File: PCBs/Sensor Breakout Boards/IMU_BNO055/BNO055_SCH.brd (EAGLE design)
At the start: 25.4 x 25.4 mm, 6 parts

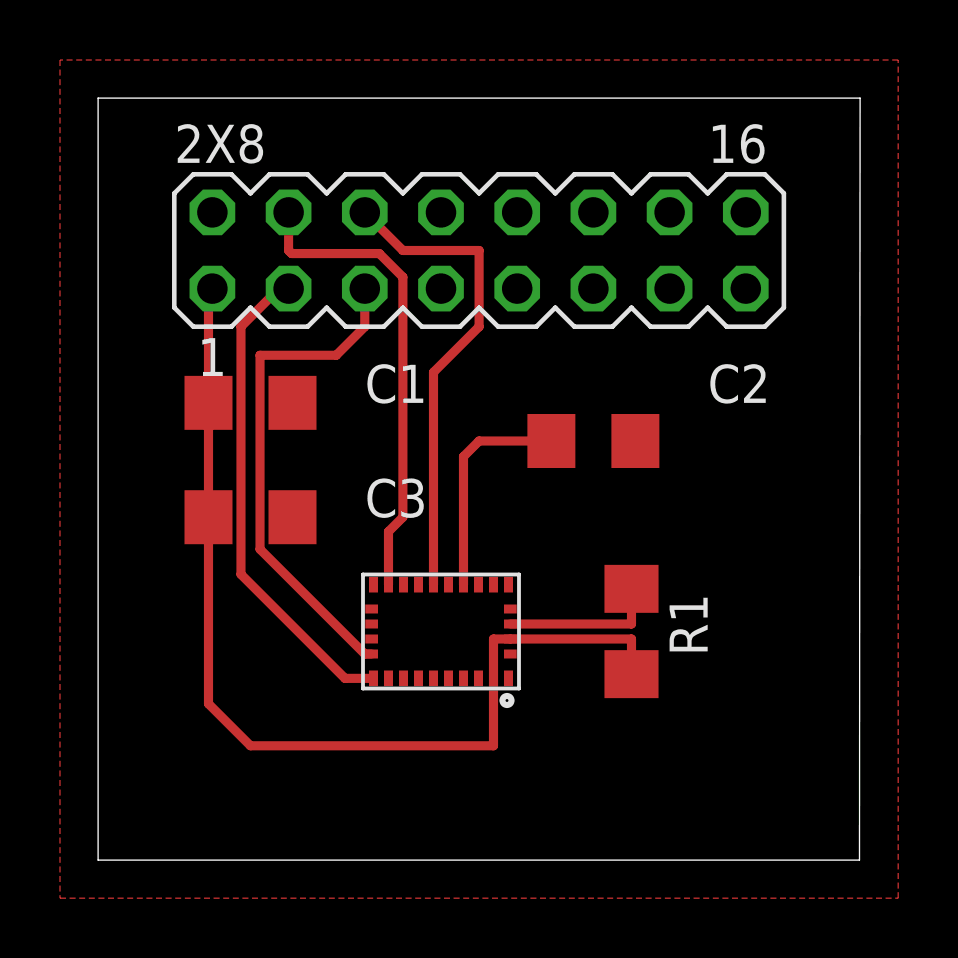
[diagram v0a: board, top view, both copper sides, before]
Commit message: Moved the caps to actually be useful
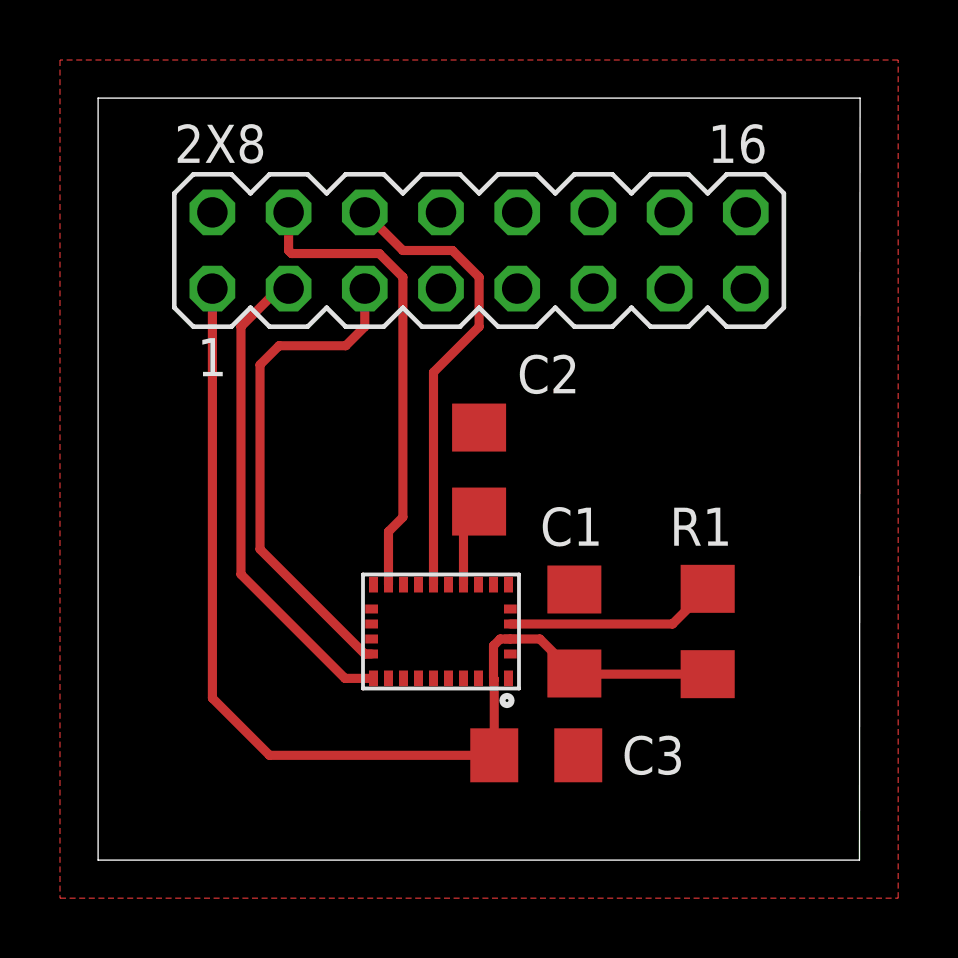
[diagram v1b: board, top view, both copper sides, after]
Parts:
- moved C1 13.2 mm to (15.9, 7.62), turned to 90 degrees
- moved C3 12.4 mm to (14.6, 3.49)
- moved C2 3.93 mm to (12.7, 13.0), turned to 90 degrees
- moved R1 2.54 mm to (20.3, 7.62)
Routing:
- net N$3: track 7.41 -> 2.65 mm
- net BOOT: track 5.21 -> 7.06 mm
- net VCC: track 33.4 -> 35.2 mm
- net RST: track 16.1 -> 15.6 mm
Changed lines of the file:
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@@
 <attribute name="VALUE" x="12.7" y="16.129" size="1.27" layer="27" ratio="10"/>
 </element>
-<element name="C1" library="rcl" library_urn="urn:adsk.eagle:library:334" package="C1206" package3d_urn="urn:adsk.eagle:package:23618/2" value="0.1 uF" x="5.08" y="15.24" smashed="yes">
-<attribute name="NAME" x="8.89" y="15.24" size="1.27" layer="25"/>
-<attribute name="POPULARITY" value="24" x="22.86" y="-6.35" size="1.778" layer="27" display="off"/>
-<attribute name="SPICEPREFIX" value="C" x="22.86" y="-6.35" size="1.778" layer="27" display="off"/>
-<attribute name="VALUE" x="-2.54" y="15.24" size="1.27" layer="27"/>
+<element name="C1" library="rcl" library_urn="urn:adsk.eagle:library:334" package="C1206" package3d_urn="urn:adsk.eagle:package:23618/2" value="0.1 uF" x="15.875" y="7.62" smashed="yes" rot="R90">
+<attribute name="NAME" x="16.8275" y="11.7475" size="1.27" layer="25" rot="R180"/>
+<attribute name="POPULARITY" value="24" x="37.465" y="25.4" size="1.778" layer="27" rot="R90" display="off"/>
+<attribute name="SPICEPREFIX" value="C" x="37.465" y="25.4" size="1.778" layer="27" rot="R90" display="off"/>
+<attribute name="VALUE" x="15.875" y="0" size="1.27" layer="27" rot="R90"/>
 </element>
-<element name="C2" library="rcl" library_urn="urn:adsk.eagle:library:334" package="C1206" package3d_urn="urn:adsk.eagle:package:23618/2" value="1 uF" x="16.51" y="13.97" smashed="yes">
-<attribute name="NAME" x="20.32" y="15.24" size="1.27" layer="25"/>
-<attribute name="POPULARITY" value="24" x="40.64" y="-7.62" size="1.778" layer="27" display="off"/>
-<attribute name="SPICEPREFIX" value="C" x="40.64" y="-7.62" size="1.778" layer="27" display="off"/>
-<attribute name="VALUE" x="20.32" y="13.97" size="1.27" layer="27"/>
+<element name="C2" library="rcl" library_urn="urn:adsk.eagle:library:334" package="C1206" package3d_urn="urn:adsk.eagle:package:23618/2" value="1 uF" x="12.7" y="13.0175" smashed="yes" rot="R90">
+<attribute name="NAME" x="13.97" y="15.5575" size="1.27" layer="25"/>
+<attribute name="POPULARITY" value="24" x="34.29" y="37.1475" size="1.778" layer="27" rot="R90" display="off"/>
+<attribute name="SPICEPREFIX" value="C" x="34.29" y="37.1475" size="1.778" layer="27" rot="R90" display="off"/>
+<attribute name="VALUE" x="12.7" y="16.8275" size="1.27" layer="27" rot="R90"/>
 </element>
-<element name="C3" library="rcl" library_urn="urn:adsk.eagle:library:334" package="C1206" package3d_urn="urn:adsk.eagle:package:23618/2" value="120 nF" x="5.08" y="11.43" smashed="yes">
-<attribute name="NAME" x="8.89" y="11.43" size="1.27" layer="25"/>
-<attribute name="POPULARITY" value="24" x="31.75" y="-2.54" size="1.778" layer="27" display="off"/>
-<attribute name="SPICEPREFIX" value="C" x="31.75" y="-2.54" size="1.778" layer="27" display="off"/>
-<attribute name="VALUE" x="2.54" y="12.7" size="1.27" layer="27"/>
+<element name="C3" library="rcl" library_urn="urn:adsk.eagle:library:334" package="C1206" package3d_urn="urn:adsk.eagle:package:23618/2" value="120 nF" x="14.605" y="3.4925" smashed="yes">
+<attribute name="NAME" x="17.4625" y="2.8575" size="1.27" layer="25"/>
+<attribute name="POPULARITY" value="24" x="41.275" y="-10.4775" size="1.778" layer="27" display="off"/>
+<attribute name="SPICEPREFIX" value="C" x="41.275" y="-10.4775" size="1.778" layer="27" display="off"/>
+<attribute name="VALUE" x="12.065" y="4.7625" size="1.27" layer="27"/>
 </element>
-<element name="R1" library="rcl" library_urn="urn:adsk.eagle:library:334" package="R1206" package3d_urn="urn:adsk.eagle:package:23540/2" value="10k" x="17.78" y="7.62" smashed="yes" rot="R270">
-<attribute name="NAME" x="19.05" y="8.89" size="1.27" layer="25" rot="R270"/>
-<attribute name="POPULARITY" value="19" x="-3.81" y="-21.59" size="1.778" layer="27" rot="R270" display="off"/>
-<attribute name="SPICEPREFIX" value="R" x="-3.81" y="-21.59" size="1.778" layer="27" rot="R270" display="off"/>
-<attribute name="VALUE" x="15.24" y="8.89" size="1.27" layer="27" rot="R270"/>
+<element name="R1" library="rcl" library_urn="urn:adsk.eagle:library:334" package="R1206" package3d_urn="urn:adsk.eagle:package:23540/2" value="10k" x="20.32" y="7.62" smashed="yes" rot="R270">
+<attribute name="NAME" x="19.05" y="10.4775" size="1.27" layer="25"/>
+<attribute name="POPULARITY" value="19" x="-1.27" y="-21.59" size="1.778" layer="27" rot="R270" display="off"/>
+<attribute name="SPICEPREFIX" value="R" x="-1.27" y="-21.59" size="1.778" layer="27" rot="R270" display="off"/>
+<attribute name="VALUE" x="17.78" y="8.89" size="1.27" layer="27" rot="R270"/>
 </element>
 <element name="BNO055" library="BNO055" package="LGA28R50P4X10_380X520X100" value="BNO055" x="11.43" y="7.62" smashed="yes" rot="R180">
@@
 <contactref element="2X8" pad="1"/>
 <contactref element="R1" pad="2"/>
-<wire x1="13.18" y1="6.0575" x2="13.18" y2="7.37" width="0.3048" layer="1"/>
-<wire x1="13.18" y1="7.37" x2="13.7425" y2="7.37" width="0.3048" layer="1"/>
-<wire x1="13.7425" y1="7.37" x2="17.78" y2="7.37" width="0.3048" layer="1"/>
-<wire x1="17.78" y1="7.37" x2="17.78" y2="6.198" width="0.3048" layer="1"/>
-<wire x1="13.18" y1="6.0575" x2="13.18" y2="3.81" width="0.3048" layer="1"/>
-<wire x1="3.68" y1="11.43" x2="3.68" y2="15.24" width="0.3048" layer="1"/>
-<wire x1="3.68" y1="15.24" x2="3.68" y2="19.05" width="0.3048" layer="1"/>
-<wire x1="3.68" y1="19.05" x2="3.81" y2="19.05" width="0.3048" layer="1"/>
-<wire x1="13.18" y1="3.81" x2="5.08" y2="3.81" width="0.3048" layer="1"/>
-<wire x1="5.08" y1="3.81" x2="3.68" y2="5.21" width="0.3048" layer="1"/>
-<wire x1="3.68" y1="5.21" x2="3.68" y2="11.43" width="0.3048" layer="1"/>
+<wire x1="13.7425" y1="7.37" x2="14.725" y2="7.37" width="0.3048" layer="1"/>
+<wire x1="14.725" y1="7.37" x2="15.875" y2="6.22" width="0.3048" layer="1"/>
+<wire x1="20.32" y1="6.198" x2="15.897" y2="6.198" width="0.3048" layer="1"/>
+<wire x1="15.897" y1="6.198" x2="15.875" y2="6.22" width="0.3048" layer="1"/>
+<wire x1="13.18" y1="6.0575" x2="13.205" y2="6.0325" width="0.3048" layer="1"/>
+<wire x1="13.205" y1="6.0325" x2="13.205" y2="3.4925" width="0.3048" layer="1"/>
+<wire x1="13.205" y1="3.4925" x2="5.715" y2="3.4925" width="0.3048" layer="1"/>
+<wire x1="5.715" y1="3.4925" x2="3.81" y2="5.3975" width="0.3048" layer="1"/>
+<wire x1="3.81" y1="5.3975" x2="3.81" y2="19.05" width="0.3048" layer="1"/>
+<wire x1="13.7425" y1="7.37" x2="13.4025" y2="7.37" width="0.3048" layer="1"/>
+<wire x1="13.18" y1="7.1475" x2="13.18" y2="6.0575" width="0.3048" layer="1"/>
+<wire x1="13.4025" y1="7.37" x2="13.18" y2="7.1475" width="0.3048" layer="1"/>
 </signal>
 <signal name="GND">
@@
 <contactref element="BNO055" pad="9"/>
 <contactref element="C2" pad="1"/>
-<wire x1="12.18" y1="9.1825" x2="12.18" y2="13.45" width="0.3048" layer="1"/>
-<wire x1="12.18" y1="13.45" x2="12.7" y2="13.97" width="0.3048" layer="1"/>
-<wire x1="12.7" y1="13.97" x2="15.11" y2="13.97" width="0.3048" layer="1"/>
+<wire x1="12.18" y1="11.0975" x2="12.7" y2="11.6175" width="0.3048" layer="1"/>
+<wire x1="12.18" y1="9.1825" x2="12.18" y2="11.0975" width="0.3048" layer="1"/>
 </signal>
 <signal name="BOOT">
 <contactref element="BNO055" pad="4"/>
 <contactref element="R1" pad="1"/>
-<wire x1="13.7425" y1="7.87" x2="17.78" y2="7.87" width="0.3048" layer="1"/>
-<wire x1="17.78" y1="7.87" x2="17.78" y2="9.042" width="0.3048" layer="1"/>
+<wire x1="13.7425" y1="7.87" x2="19.148" y2="7.87" width="0.3048" layer="1"/>
+<wire x1="19.148" y1="7.87" x2="20.32" y2="9.042" width="0.3048" layer="1"/>
 </signal>
 <signal name="SDA">
@@
 <wire x1="9.1175" y1="6.87" x2="8.89" y2="6.87" width="0.3048" layer="1"/>
 <wire x1="8.89" y1="6.87" x2="5.3975" y2="10.3625" width="0.3048" layer="1"/>
-<wire x1="5.3975" y1="16.8275" x2="7.9375" y2="16.8275" width="0.3048" layer="1"/>
-<wire x1="7.9375" y1="16.8275" x2="8.89" y2="17.78" width="0.3048" layer="1"/>
 <wire x1="8.89" y1="17.78" x2="8.89" y2="19.05" width="0.3048" layer="1"/>
-<wire x1="5.3975" y1="10.3625" x2="5.3975" y2="16.8275" width="0.3048" layer="1"/>
+<wire x1="5.3975" y1="10.3625" x2="5.3975" y2="16.51" width="0.3048" layer="1"/>
+<wire x1="5.3975" y1="16.51" x2="6.0325" y2="17.145" width="0.3048" layer="1"/>
+<wire x1="8.255" y1="17.145" x2="8.89" y2="17.78" width="0.3048" layer="1"/>
+<wire x1="6.0325" y1="17.145" x2="8.255" y2="17.145" width="0.3048" layer="1"/>
 </signal>
 <signal name="INT">
@@
 <wire x1="11.18" y1="9.1825" x2="11.18" y2="16.26" width="0.3048" layer="1"/>
 <wire x1="11.18" y1="16.26" x2="12.7" y2="17.78" width="0.3048" layer="1"/>
-<wire x1="12.7" y1="17.78" x2="12.7" y2="20.32" width="0.3048" layer="1"/>
-<wire x1="12.7" y1="20.32" x2="11.43" y2="20.32" width="0.3048" layer="1"/>
-<wire x1="11.43" y1="20.32" x2="11.04763125" y2="20.32" width="0.3048" layer="1"/>
-<wire x1="11.04763125" y1="20.32" x2="10.16" y2="20.32" width="0.3048" layer="1"/>
 <wire x1="10.16" y1="20.32" x2="8.89" y2="21.59" width="0.3048" layer="1"/>
+<wire x1="12.7" y1="17.78" x2="12.7" y2="19.43236875" width="0.3048" layer="1"/>
+<wire x1="12.7" y1="19.43236875" x2="11.81236875" y2="20.32" width="0.3048" layer="1"/>
+<wire x1="11.81236875" y1="20.32" x2="10.16" y2="20.32" width="0.3048" layer="1"/>
 </signal>
 </signals>
